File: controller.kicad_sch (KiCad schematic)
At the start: 0 parts

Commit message: Controller selection
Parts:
- added U10: STM32C031K6Tx, Package_QFP:LQFP-32_7x7mm_P0.8mm, symbol MCU_ST_STM32C0:STM32C031K6Tx
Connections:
- new net GND: U10.5 (VSS)
- new net VCC: U10.4 (VDD)

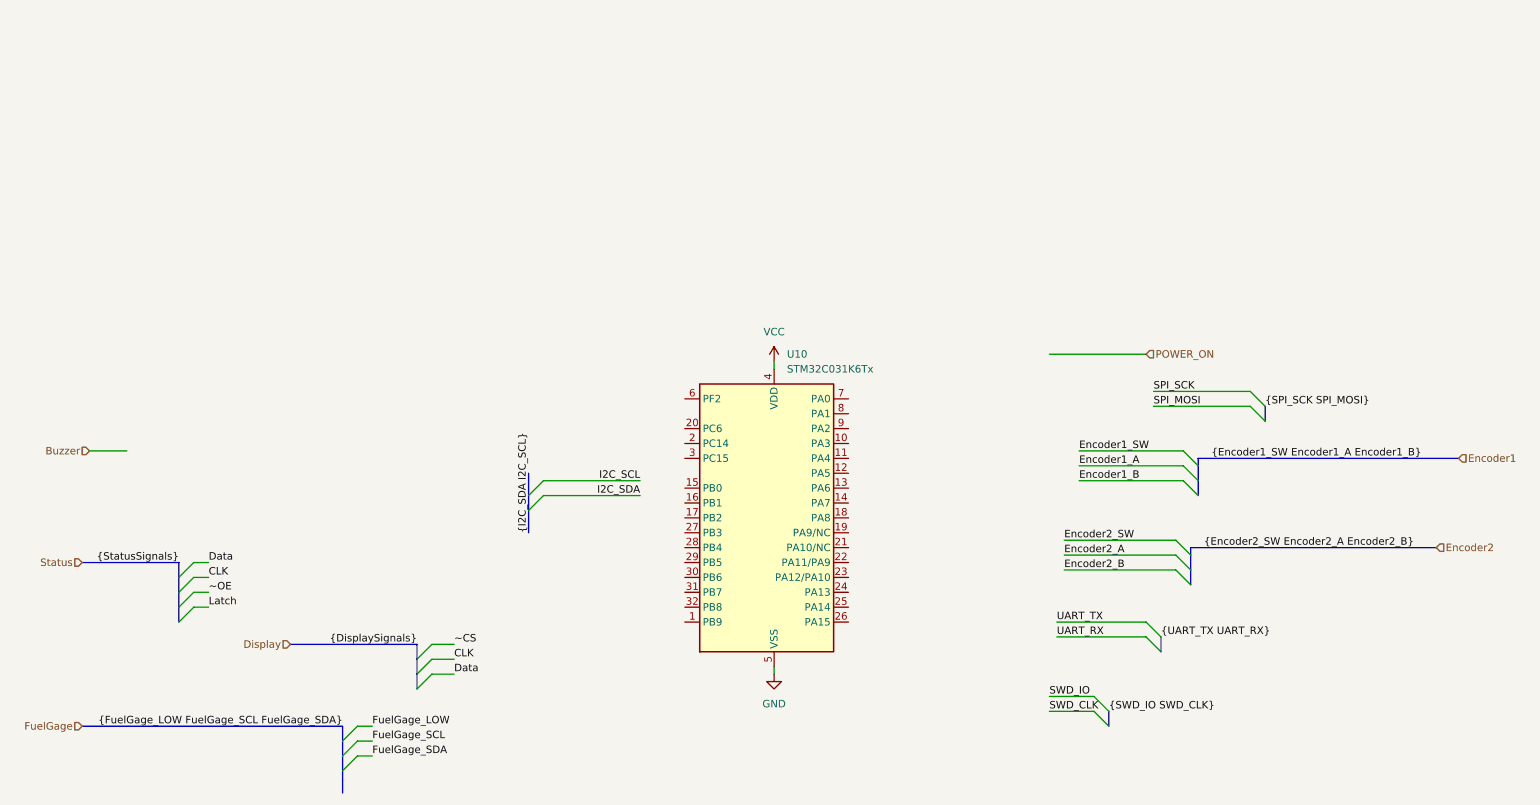
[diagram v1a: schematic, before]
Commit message: Controller wiring and schematic semantics
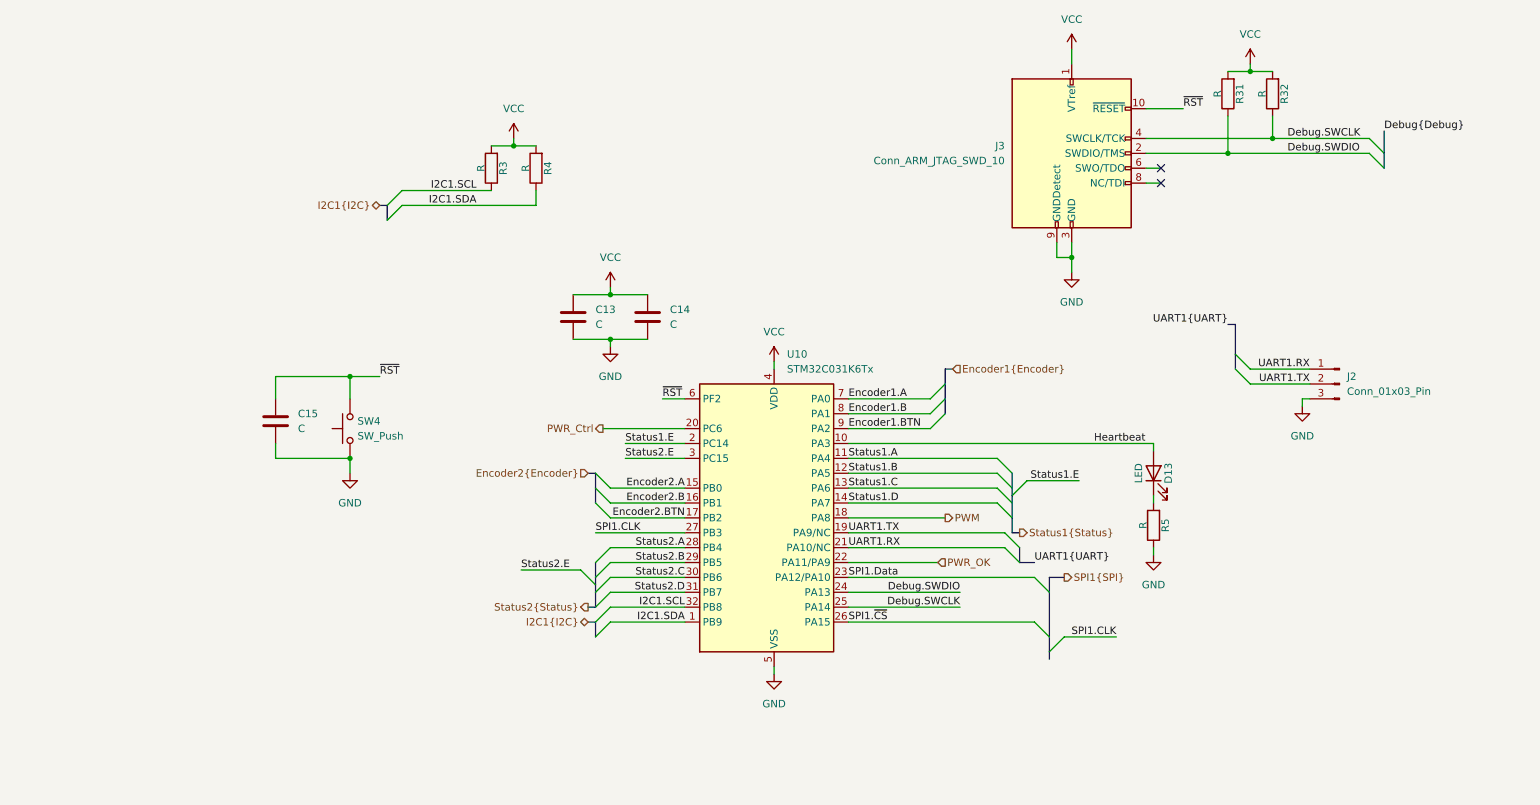
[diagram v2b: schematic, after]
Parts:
- added C13, C14, C15: C, symbol Device:C
- added D13: LED, symbol Device:LED
- added J2: Conn_01x03_Pin, symbol Connector:Conn_01x03_Pin
- added J3: Conn_ARM_JTAG_SWD_10, symbol Connector:Conn_ARM_JTAG_SWD_10
- added R3, R31, R32, R4, R5: R, symbol Device:R
- added SW4: SW_Push, symbol Switch:SW_Push
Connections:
- net GND: now also C13.2, C14.2, C15.2, J2.3 (Pin_3), J3.3 (GND), J3.5 (GND), J3.9 (GNDDetect), R5.1, SW4.1
- net VCC: now also C13.1, C14.1, J3.1 (VTref), R3.2, R31.2, R32.2, R4.2
- net I2C1.SDA: now reaches U10.1 (PB9)
- net I2C1.SDA: now also R4.1
- net Heartbeat: now reaches U10.10 (PA3)
- net Heartbeat: now also D13.2 (A)
- net Status1.A: now reaches U10.11 (PA4)
- net Status1.B: now reaches U10.12 (PA5)
- net Status1.C: now reaches U10.13 (PA6)
- net Status1.D: now reaches U10.14 (PA7)
- net Encoder2.A: now reaches U10.15 (PB0)
- net Encoder2.B: now reaches U10.16 (PB1)
- net Encoder2.BTN: now reaches U10.17 (PB2)
- net PWM: now reaches U10.18 (PA8)
- net UART1.TX: now reaches U10.19 (PA9/NC)
- net UART1.TX: now also J2.2 (Pin_2)
- net Status1.E: now reaches U10.2 (PC14)
- net PWR_Ctrl: now reaches U10.20 (PC6)
- net UART1.RX: now reaches U10.21 (PA10/NC)
- net UART1.RX: now also J2.1 (Pin_1)
- net PWR_OK: now reaches U10.22 (PA11/PA9)
- net SPI1.Data: now reaches U10.23 (PA12/PA10)
- net Debug.SWDIO: now reaches U10.24 (PA13)
- net Debug.SWDIO: now also J3.2 (SWDIO/TMS), R31.1
- net Debug.SWCLK: now reaches U10.25 (PA14)
- net Debug.SWCLK: now also J3.4 (SWCLK/TCK), R32.1
- net SPI1.~{CS}: now reaches U10.26 (PA15)
- net SPI1.CLK: now reaches U10.27 (PB3)
- net Status2.A: now reaches U10.28 (PB4)
- net Status2.B: now reaches U10.29 (PB5)
- net Status2.E: now reaches U10.3 (PC15)
- net Status2.C: now reaches U10.30 (PB6)
- net Status2.D: now reaches U10.31 (PB7)
- net I2C1.SCL: now reaches U10.32 (PB8)
- net I2C1.SCL: now also R3.1
- net ~{RST}: now reaches U10.6 (PF2)
- net ~{RST}: now also C15.1, J3.10 (~{RESET}), SW4.2
- net Encoder1.A: now reaches U10.7 (PA0)
- net Encoder1.B: now reaches U10.8 (PA1)
- net Encoder1.BTN: now reaches U10.9 (PA2)
- new net: D13.1 (K), R5.2
- no-connect marks 0 -> 2

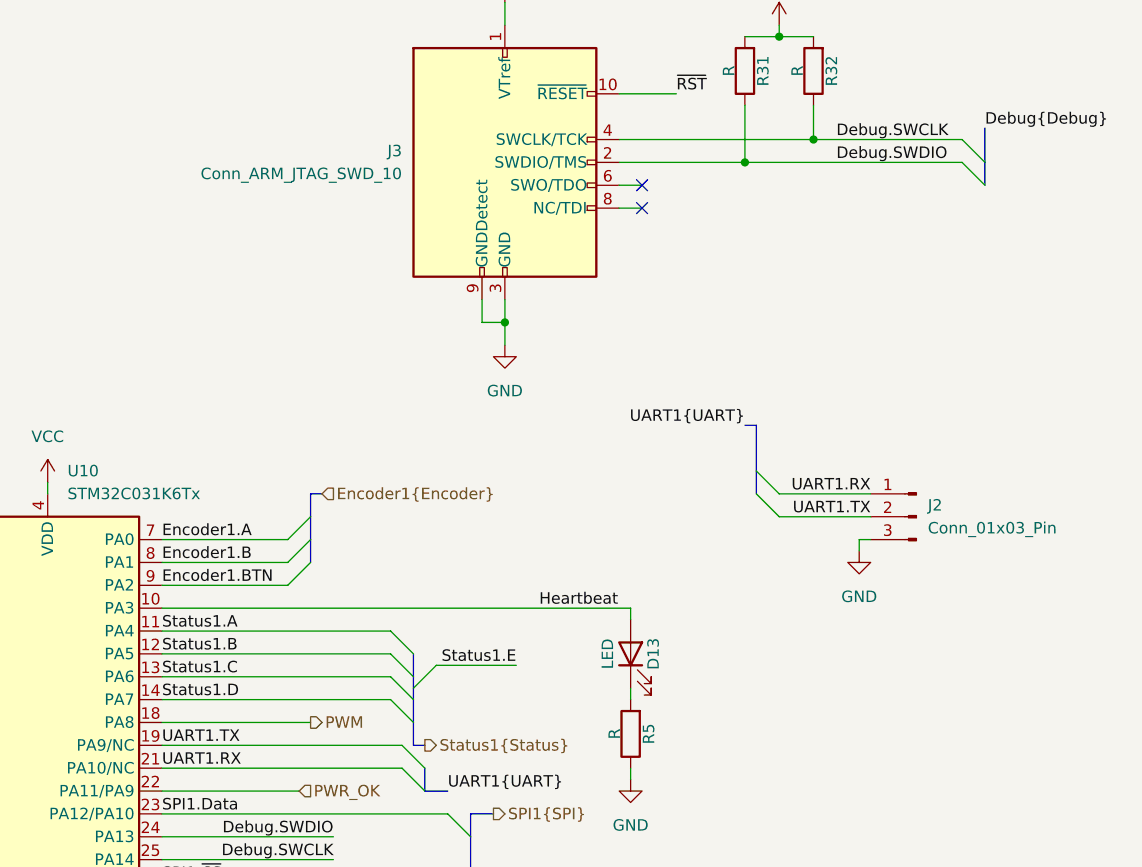
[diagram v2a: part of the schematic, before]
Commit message: LED descriptions - Status LEDs could use some more work
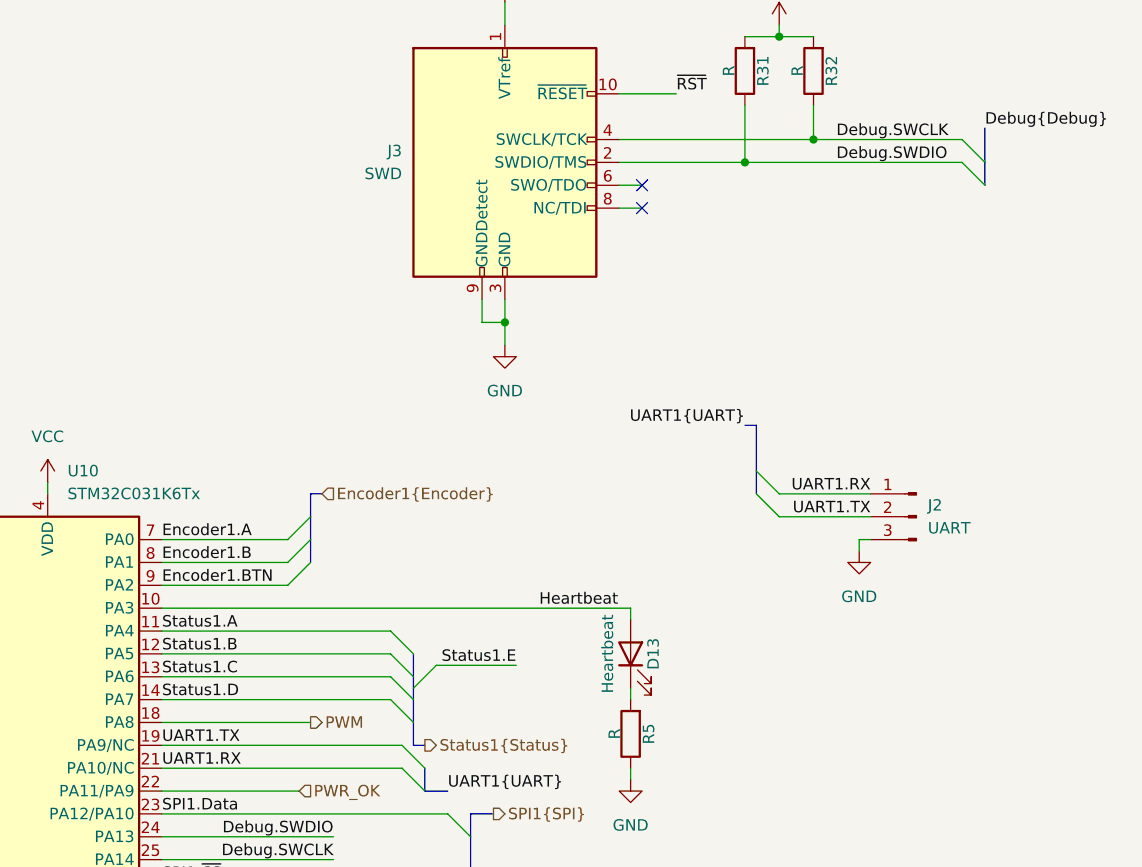
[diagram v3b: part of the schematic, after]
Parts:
- D13: value LED -> Heartbeat
- J2: value Conn_01x03_Pin -> UART
- J3: value Conn_ARM_JTAG_SWD_10 -> SWD
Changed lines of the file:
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@@
 			)
 		)
-		(property "Value" "Conn_01x03_Pin"
+		(property "Value" "UART"
 			(at 246.38 77.4699 0)
 			(effects
@@
 			)
 		)
-		(property "Value" "Conn_ARM_JTAG_SWD_10"
+		(property "Value" "SWD"
 			(at 187.96 38.0999 0)
 			(effects
@@
 			)
 		)
-		(property "Value" "LED"
+		(property "Value" "Heartbeat"
 			(at 210.82 91.44 0)
 			(effects

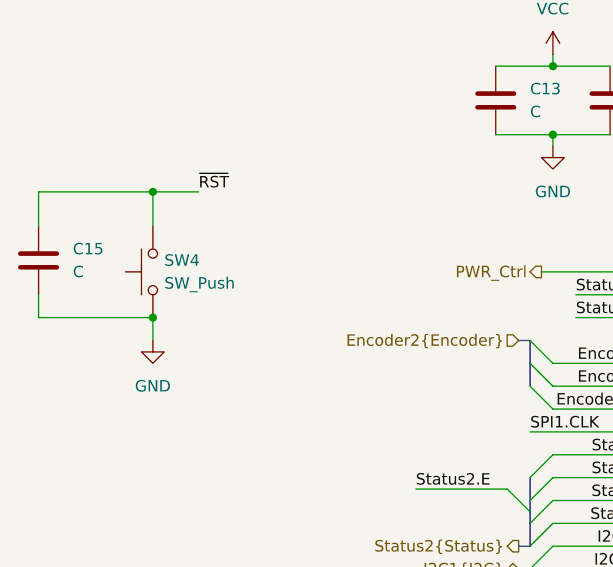
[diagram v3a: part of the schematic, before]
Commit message: Initial component placement
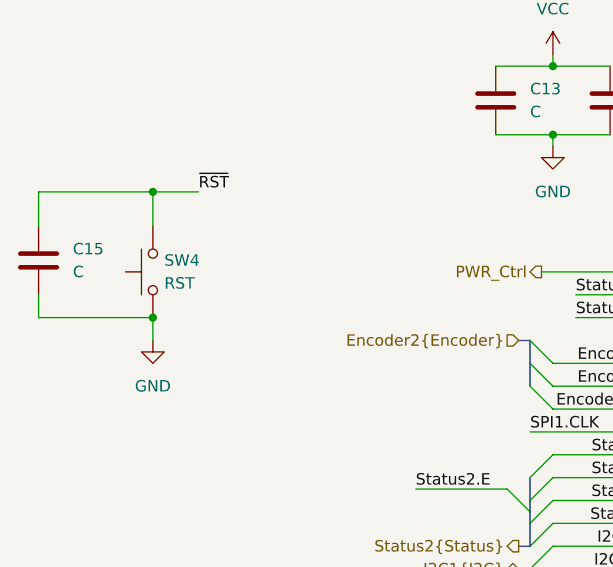
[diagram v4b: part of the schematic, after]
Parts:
- C13, C14, C15: footprint (none) -> Capacitor_SMD:C_0805_2012Metric_Pad1.18x1.45mm_HandSolder
- D13: footprint (none) -> LED_SMD:LED_0805_2012Metric_Pad1.15x1.40mm_HandSolder
- J2: footprint (none) -> Connector_PinHeader_2.54mm:PinHeader_1x03_P2.54mm_Vertical_SMD_Pin1Left
- J3: footprint (none) -> Connector_PinHeader_1.27mm:PinHeader_2x05_P1.27mm_Vertical_SMD
- R3, R31, R32, R4, R5: footprint (none) -> Resistor_SMD:R_0805_2012Metric_Pad1.20x1.40mm_HandSolder
- SW4: value SW_Push -> RST; footprint (none) -> Button_Switch_SMD:SW_SPST_PTS647_Sx38
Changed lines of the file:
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@@
 			)
 		)
-		(property "Footprint" ""
+		(property "Footprint" "Resistor_SMD:R_0805_2012Metric_Pad1.20x1.40mm_HandSolder"
 			(at 235.458 26.67 90)
 			(effects
@@
 			)
 		)
-		(property "Footprint" ""
+		(property "Footprint" "Resistor_SMD:R_0805_2012Metric_Pad1.20x1.40mm_HandSolder"
 			(at 215.138 100.33 90)
 			(effects
@@
 			)
 		)
-		(property "Footprint" ""
+		(property "Footprint" "Resistor_SMD:R_0805_2012Metric_Pad1.20x1.40mm_HandSolder"
 			(at 109.728 39.37 90)
 			(effects
@@
 			)
 		)
-		(property "Value" "SW_Push"
+		(property "Value" "RST"
 			(at 77.47 85.0899 90)
 			(effects
@@
 			)
 		)
-		(property "Footprint" ""
+		(property "Footprint" "Button_Switch_SMD:SW_SPST_PTS647_Sx38"
 			(at 71.12 83.82 0)
 			(effects
@@
 			)
 		)
-		(property "Footprint" ""
+		(property "Footprint" "Connector_PinHeader_2.54mm:PinHeader_1x03_P2.54mm_Vertical_SMD_Pin1Left"
 			(at 245.11 76.2 0)
 			(effects
@@
 			)
 		)
-		(property "Footprint" ""
+		(property "Footprint" "Connector_PinHeader_1.27mm:PinHeader_2x05_P1.27mm_Vertical_SMD"
 			(at 199.39 36.83 0)
 			(effects
@@
 			)
 		)
-		(property "Footprint" ""
+		(property "Footprint" "Capacitor_SMD:C_0805_2012Metric_Pad1.18x1.45mm_HandSolder"
 			(at 115.2652 68.58 0)
 			(effects
@@
 			)
 		)
-		(property "Footprint" ""
+		(property "Footprint" "Capacitor_SMD:C_0805_2012Metric_Pad1.18x1.45mm_HandSolder"
 			(at 127.9652 68.58 0)
 			(effects
@@
 			)
 		)
-		(property "Footprint" ""
+		(property "Footprint" "Capacitor_SMD:C_0805_2012Metric_Pad1.18x1.45mm_HandSolder"
 			(at 64.4652 86.36 0)
 			(effects
@@
 			)
 		)
-		(property "Footprint" ""
+		(property "Footprint" "Resistor_SMD:R_0805_2012Metric_Pad1.20x1.40mm_HandSolder"
 			(at 102.108 39.37 90)
 			(effects
@@
 			)
 		)
-		(property "Footprint" ""
+		(property "Footprint" "LED_SMD:LED_0805_2012Metric_Pad1.15x1.40mm_HandSolder"
 			(at 213.36 91.44 0)
 			(effects
@@
 			)
 		)
-		(property "Footprint" ""
+		(property "Footprint" "Resistor_SMD:R_0805_2012Metric_Pad1.20x1.40mm_HandSolder"
 			(at 227.838 26.67 90)
 			(effects

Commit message: Initial layout
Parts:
- removed J2: UART, Connector_PinHeader_2.54mm:PinHeader_1x03_P2.54mm_Vertical_SMD_Pin1Left, symbol Connector:Conn_01x03_Pin
- removed J3: SWD, Connector_PinHeader_1.27mm:PinHeader_2x05_P1.27mm_Vertical_SMD, symbol Connector:Conn_ARM_JTAG_SWD_10
- added J2: Debug, Connector_PinHeader_2.54mm:PinHeader_2x03_P2.54mm_Vertical_SMD, symbol Connector_Generic:Conn_02x03_Odd_Even
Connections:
- net Debug.SWCLK: now also J2.4 (Pin_4)
- net Debug.SWDIO: now also J2.6 (Pin_6)
- net GND: now also J2.1 (Pin_1)
- net UART1.RX: now also J2.5 (Pin_5)
- net UART1.TX: now also J2.3 (Pin_3)
- net ~{RST}: now also J2.2 (Pin_2)
- no-connect marks 2 -> 0
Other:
- moved on the sheet: R31, R32

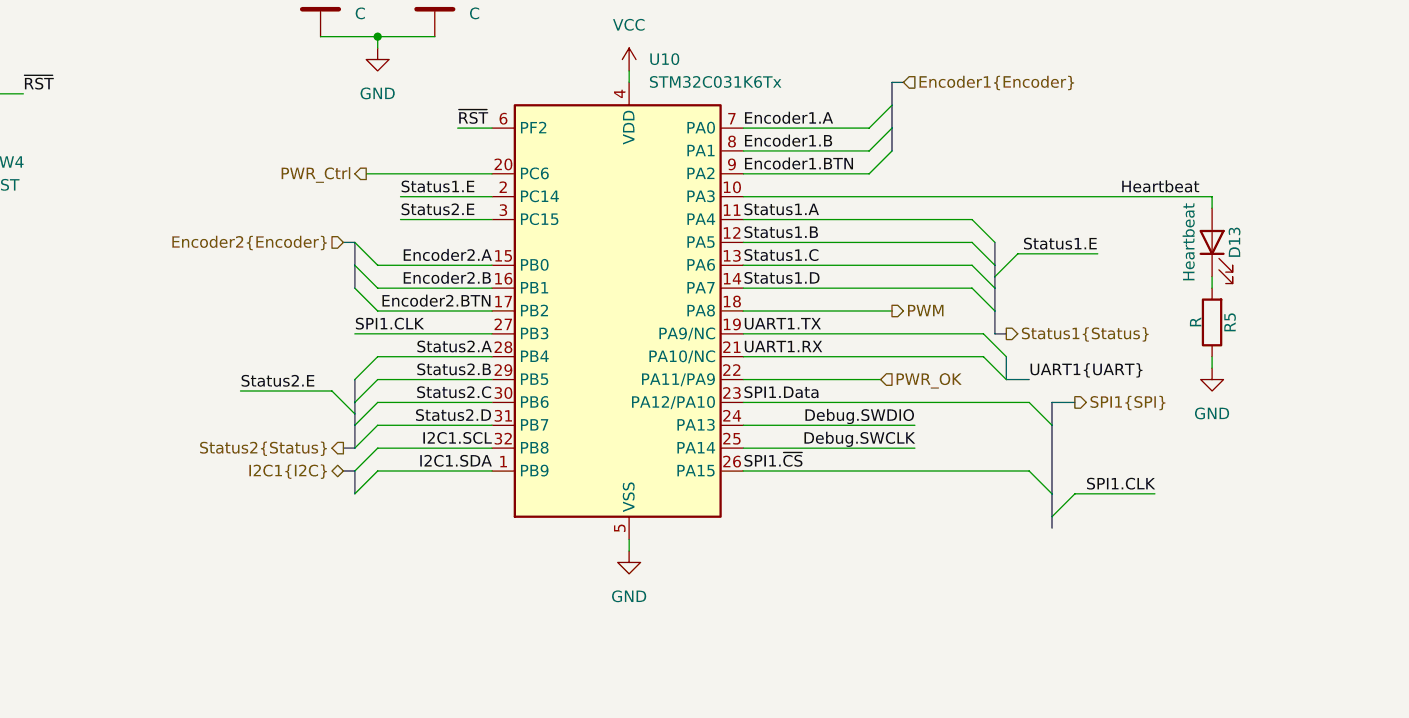
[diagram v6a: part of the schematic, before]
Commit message: Constant current sink to status LEDs and rewiring controller
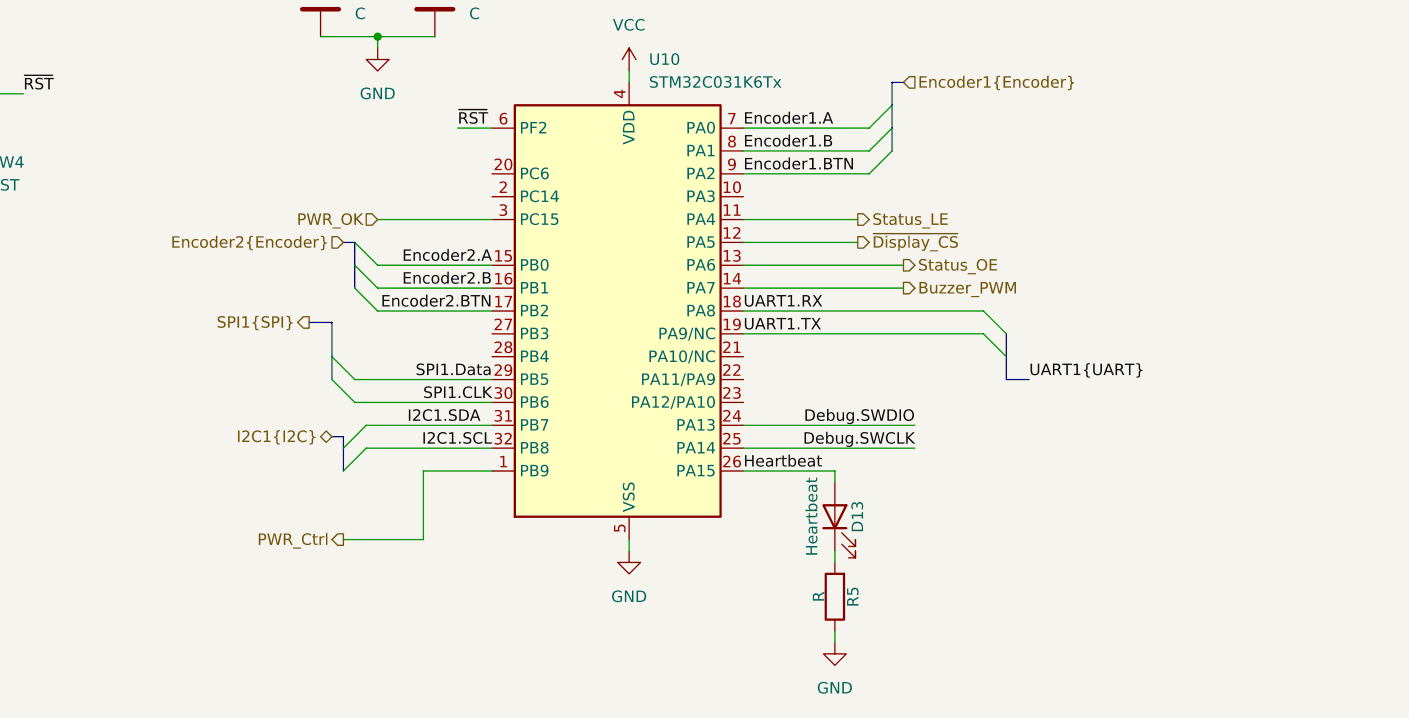
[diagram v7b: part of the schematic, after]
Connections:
- net PWM is gone; now on net UART1.RX: U10.18 (PA8)
- net SPI1.~{CS} is gone; now on net Heartbeat: U10.26 (PA15)
- net Status2.B is gone; now on net SPI1.Data: U10.29 (PB5)
- net Status2.C is gone; now on net SPI1.CLK: U10.30 (PB6)
- net Status2.D is gone; now on net I2C1.SDA: U10.31 (PB7)
- net Status2.E is gone; now on net PWR_OK: U10.3 (PC15)
- net Heartbeat: no longer U10.10 (PA3)
- net I2C1.SDA: no longer U10.1 (PB9)
- net PWR_Ctrl: now also U10.1 (PB9); no longer U10.20 (PC6)
- net PWR_OK: no longer U10.22 (PA11/PA9)
- net SPI1.CLK: no longer U10.27 (PB3)
- net SPI1.Data: no longer U10.23 (PA12/PA10)
- net UART1.RX: no longer U10.21 (PA10/NC)
- net Status1.A renamed Status_LE
- net Status1.B renamed ~{Display_CS}
- net Status1.C renamed Status_OE
- net Status1.D renamed Buzzer_PWM
- net Status1.E: no longer names the net of U10.2 (PC14)
- net Status2.A: no longer names the net of U10.28 (PB4)
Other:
- moved on the sheet: D13, R5
